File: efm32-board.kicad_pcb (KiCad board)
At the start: 2 copper layers, 18.8 x 51.8 mm, 30 parts, among them J1 Conn_01x20, J2 Conn_01x20, J3 USB_OTG, J4 Conn_02x03_Odd_Even, J5 Conn_01x20, J6 Conn_01x20, SW1 reset, SW2 reset, U1 EFM32HG-48LQFP, U2 SPX3819M5-L-3-3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

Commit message: Add +5v input diode array for split vbus and vin
Signed-off-by: Martin Ribelotta <martinribelotta@gmail.com>
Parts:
- added D2: PMEG2005CT, TO_SOT_Packages_SMD:SOT-23, F.Cu at (131.4, 73.9)
- moved J3 4.27 mm to (125.1, 71.7)
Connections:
- J2 pad 1: +5V -> /vin
- J3 pad 1: +5V -> /vusb
- J5 pad 1: +5V -> /vin
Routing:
- net +5V: track 23.0 -> 14.0 mm
- net /vusb: track 0.00 -> 6.62 mm
- net /vin: track 0.00 -> 4.95 mm
- net /B_USB-: track 4.10 -> 5.93 mm
- net /PF0/SWCLK: track 26.1 -> 24.8 mm
- net +3V3: track 110.5 -> 109.2 mm

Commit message: Corrections and fixeds
Signed-off-by: Martin Ribelotta <martinribelotta@gmail.com>
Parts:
- added C12: 4.7u, Capacitors_SMD:C_0603, F.Cu at (129.2, 86.9)
- moved C7 2.56 mm to (127.8, 86.9)
- moved C6 0.27 mm to (131.5, 91.0)
- moved C8 0.27 mm to (132.8, 91.0)
- moved C9 0.11 mm to (132.1, 89.0)
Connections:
- C7 pad 1: +3V3 -> Net-(C7-Pad1)
- J4 pad 2: +5V -> Net-(J4-Pad2)
- U1 pad 33: +3V3 -> /vusb
- U1 pad 34: +3V3 -> Net-(C7-Pad1)
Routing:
- net /vusb: track 6.62 -> 25.3 mm, vias 0 -> 2
- net +3V3: track 109.2 -> 123.8 mm, vias 1 -> 0
- net +5V: track 14.0 -> 7.17 mm
- net Net-(C7-Pad1): track 0.00 -> 5.86 mm
- net /USB-: track 9.57 -> 10.8 mm
- net /PF0/SWCLK: track 24.8 -> 25.5 mm
- net /USB+: track 9.34 -> 9.85 mm

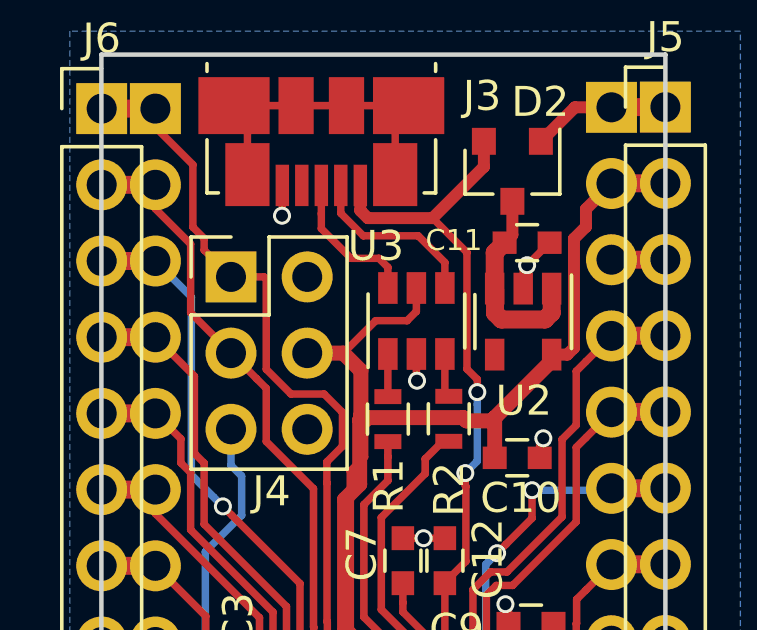
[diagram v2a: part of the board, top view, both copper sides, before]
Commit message: Add jump to pins 2-4 on J4 (SWD)
Signed-off-by: Martin Ribelotta <martinribelotta@gmail.com>
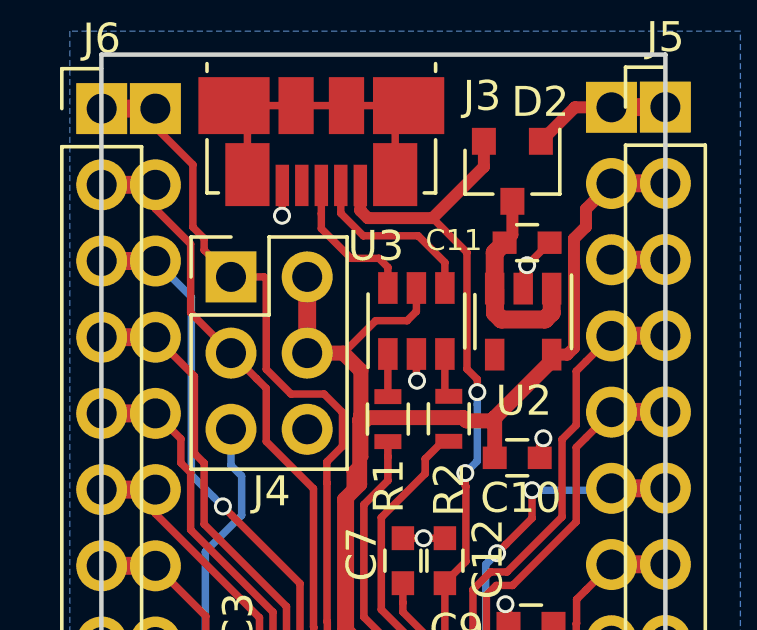
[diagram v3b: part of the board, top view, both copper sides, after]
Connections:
- J4 pad 2: Net-(J4-Pad2) -> +3V3
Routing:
- net +3V3: track 123.8 -> 126.3 mm
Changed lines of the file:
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@@
     (thickness 1.6)
     (drawings 4)
-    (tracks 641)
+    (tracks 642)
     (zones 0)
     (modules 32)
-    (nets 52)
+    (nets 51)
   )
   (page A4)
@@
   (net 49 /vin)
   (net 50 "Net-(C7-Pad1)")
-  (net 51 "Net-(J4-Pad2)")
   (net_class Default "This is the default net class."
     (clearance 0.2)
@@
     (add_net "Net-(D3-Pad2)")
     (add_net "Net-(J3-Pad6)")
-    (add_net "Net-(J4-Pad2)")
     (add_net "Net-(R1-Pad1)")
     (add_net "Net-(R2-Pad1)")
@@
       (net 13 /PF1/SWDIO))
     (pad 2 thru_hole oval (at 2.54 0) (size 1.7 1.7) (drill 1) (layers *.Cu *.Mask)
-      (net 51 "Net-(J4-Pad2)"))
+      (net 3 +3V3))
     (pad 1 thru_hole rect (at 0 0) (size 1.7 1.7) (drill 1) (layers *.Cu *.Mask)
       (net 12 /PF0/SWCLK))
@@
   (segment (start 123.768 75.385) (end 123.758 75.395) (width 0.25) (layer F.Cu) (net 2))
   (via (at 123.758 75.395) (size 0.6) (drill 0.4) (layers F.Cu B.Cu) (net 2))
+  (segment (start 124.598 77.435) (end 124.598 79.975) (width 0.6) (layer F.Cu) (net 3))
   (segment (start 130.848 82.135) (end 130.848 82.13) (width 0.5) (layer F.Cu) (net 3))
   (segment (start 129.798011 82.125001) (end 126.477999 82.125001) (width 0.5) (layer F.Cu) (net 3))

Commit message: Change usb resistors from 22R to 15R
Signed-off-by: Martin Ribelotta <martinribelotta@gmail.com>
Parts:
- R1, R2: value 22R -> 15R
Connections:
- J3 pad 4: (no net) -> Net-(J3-Pad4)
- U2 pad 4: (no net) -> Net-(U2-Pad4)
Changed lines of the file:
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@@
     (zones 0)
     (modules 32)
-    (nets 51)
+    (nets 53)
   )
   (page A4)
@@
   (net 49 /vin)
   (net 50 "Net-(C7-Pad1)")
+  (net 51 "Net-(J3-Pad4)")
+  (net 52 "Net-(U2-Pad4)")
   (net_class Default "This is the default net class."
     (clearance 0.2)
@@
     (add_net "Net-(D1-Pad2)")
     (add_net "Net-(D3-Pad2)")
+    (add_net "Net-(J3-Pad4)")
     (add_net "Net-(J3-Pad6)")
     (add_net "Net-(R1-Pad1)")
     (add_net "Net-(R2-Pad1)")
+    (add_net "Net-(U2-Pad4)")
   )
   (module Capacitors_SMD:C_0603 (layer F.Cu)
@@
     (pad 5 smd rect (at 1.1 -0.95 270) (size 1.06 0.65) (layers F.Cu F.Paste F.Mask)
       (net 3 +3V3))
-    (pad 4 smd rect (at 1.1 0.95 270) (size 1.06 0.65) (layers F.Cu F.Paste F.Mask))
+    (pad 4 smd rect (at 1.1 0.95 270) (size 1.06 0.65) (layers F.Cu F.Paste F.Mask)
+      (net 52 "Net-(U2-Pad4)"))
     (pad 3 smd rect (at -1.1 0.95 270) (size 1.06 0.65) (layers F.Cu F.Paste F.Mask)
       (net 1 +5V))
@@
       (effects (font (size 1 1) (thickness 0.15)))
     )
-    (fp_text value 22R (at 0 1.5 270) (layer F.Fab)
+    (fp_text value 15R (at 0 1.5 270) (layer F.Fab)
       (effects (font (size 1 1) (thickness 0.15)))
     )
@@
       (effects (font (size 1 1) (thickness 0.15)))
     )
-    (fp_text value 22R (at 0 1.5 270) (layer F.Fab)
+    (fp_text value 15R (at 0 1.5 270) (layer F.Fab)
       (effects (font (size 1 1) (thickness 0.15)))
     )
@@
     (pad 5 smd rect (at 1.3 -2.66 180) (size 0.45 1.38) (layers F.Cu F.Paste F.Mask)
       (net 2 GND))
-    (pad 4 smd rect (at 0.65 -2.66 180) (size 0.45 1.38) (layers F.Cu F.Paste F.Mask))
+    (pad 4 smd rect (at 0.65 -2.66 180) (size 0.45 1.38) (layers F.Cu F.Paste F.Mask)
+      (net 51 "Net-(J3-Pad4)"))
     (pad 3 smd rect (at 0 -2.66 180) (size 0.45 1.38) (layers F.Cu F.Paste F.Mask)
       (net 44 /B_USB+))

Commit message: Various fixes for release
Signed-off-by: Martin Ribelotta <martinribelotta@gmail.com>
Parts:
- J4: value Conn_02x03_Odd_Even -> SWD; footprint Pin_Headers:Pin_Header_Straight_2x03_Pitch2.54mm -> Pin_Headers:Pin_Header_Straight_2x02_Pitch2.54mm_SMD
- moved J4 4.23 mm to (123.4, 81.5), turned to 270 degrees
- moved C2 0.31 mm to (121.6, 100.6)
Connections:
- J2 pad 2: +3V3 -> GND
- J2 pad 3: GND -> +3V3
- J3 pad 4: Net-(J3-Pad4) -> (no net)
- J4 pad 2: +3V3 -> GND
- J4 pad 4: +3V3 -> /nRESET
- J5 pad 2: +3V3 -> GND
- J5 pad 3: GND -> +3V3
- U2 pad 4: Net-(U2-Pad4) -> (no net)
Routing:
- net +3V3: track 126.3 -> 119.0 mm
- net /nRESET: track 58.8 -> 55.6 mm, vias 3 -> 4
- net GND: track 36.6 -> 38.6 mm, vias 16 -> 17
- net /PF0/SWCLK: track 25.5 -> 24.5 mm
- net /PF1/SWDIO: track 21.4 -> 22.1 mm
- net /PF2: track 19.1 -> 19.4 mm, vias 1 -> 0
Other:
- board text added: "PA7"
- board text added: "PB8"
- board text added: "PWR"
- board text added: "RST"

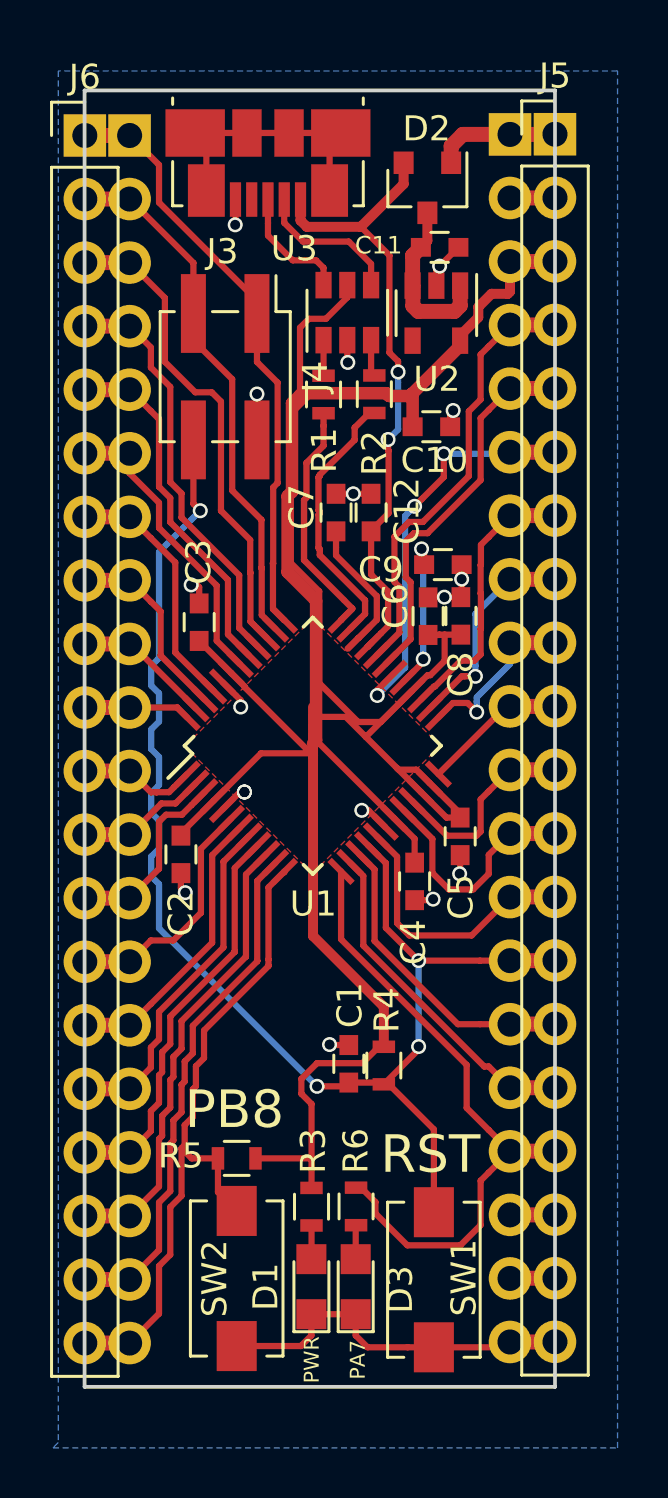
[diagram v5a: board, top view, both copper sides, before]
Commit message: Add +3v3 on pin 18 (previous GND) for prototyping convenience
Signed-off-by: Martin Ribelotta <martinribelotta@gmail.com>
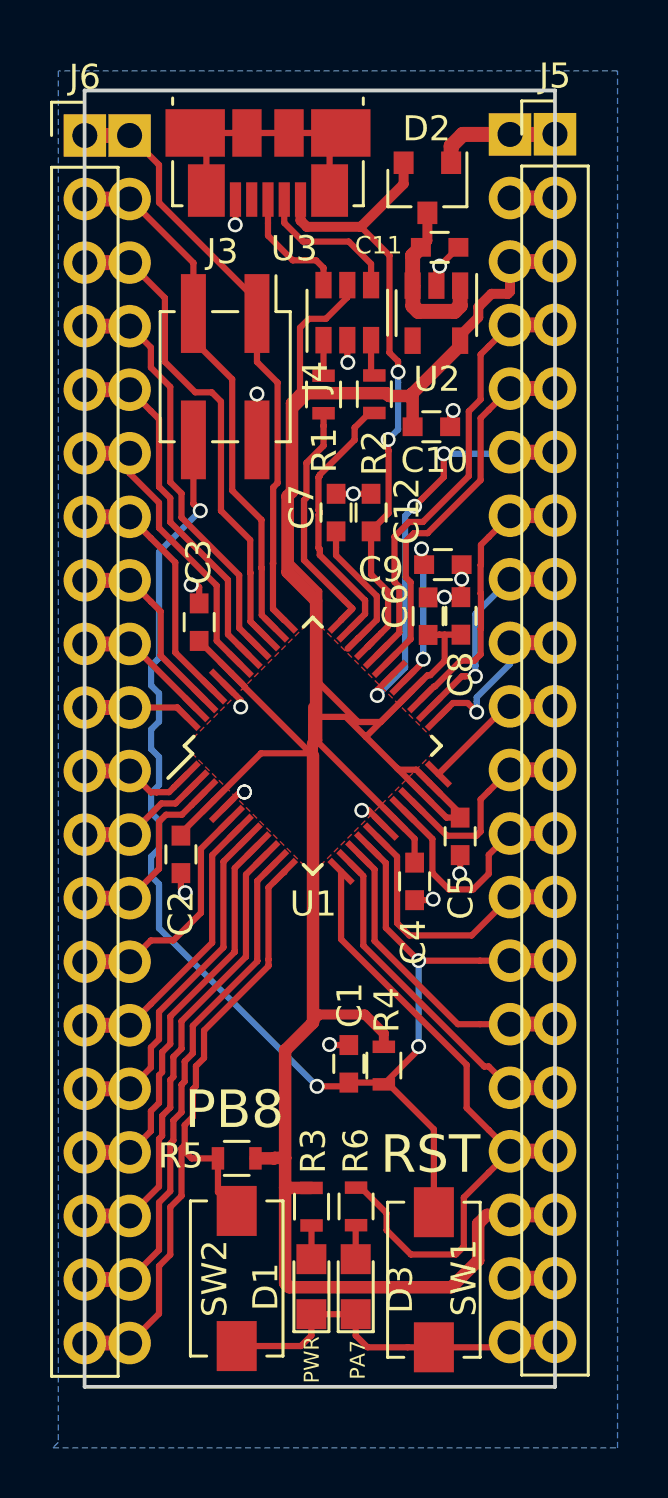
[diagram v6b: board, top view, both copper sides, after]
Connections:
- J2 pad 18: GND -> +3V3
- J5 pad 18: GND -> +3V3
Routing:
- net +3V3: track 119.0 -> 136.2 mm
- net GND: track 38.6 -> 36.8 mm
- net /PA8: track 25.8 -> 26.3 mm
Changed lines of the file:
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@@
     (thickness 1.6)
     (drawings 8)
-    (tracks 663)
+    (tracks 671)
     (zones 0)
     (modules 32)
@@
       (net 32 /PA8))
     (pad 18 thru_hole oval (at 0 43.18) (size 1.7 1.7) (drill 1) (layers *.Cu *.Mask)
-      (net 2 GND))
+      (net 3 +3V3))
     (pad 19 thru_hole oval (at 0 45.72) (size 1.7 1.7) (drill 1) (layers *.Cu *.Mask)
       (net 2 GND))
@@
       (net 32 /PA8))
     (pad 18 thru_hole oval (at 0 -43.18 180) (size 1.7 1.7) (drill 1) (layers *.Cu *.Mask)
-      (net 2 GND))
+      (net 3 +3V3))
     (pad 19 thru_hole oval (at 0 -45.72 180) (size 1.7 1.7) (drill 1) (layers *.Cu *.Mask)
       (net 2 GND))
@@
   (segment (start 123.768 75.385) (end 123.758 75.395) (width 0.25) (layer F.Cu) (net 2))
   (via (at 123.758 75.395) (size 0.6) (drill 0.4) (layers F.Cu B.Cu) (net 2))
+  (segment (start 134.740619 114.9625) (end 136.5305 114.9625) (width 0.6) (layer F.Cu) (net 3))
+  (segment (start 136.5305 114.9625) (end 136.538 114.955) (width 0.6) (layer F.Cu) (net 3))
+  (segment (start 132.398 117.855) (end 133.468 116.785) (width 0.5) (layer F.Cu) (net 3))
+  (segment (start 133.468 116.785) (end 133.468 115.315) (width 0.5) (layer F.Cu) (net 3))
+  (segment (start 125.753 113.875) (end 125.753 117.692501) (width 0.5) (layer F.Cu) (net 3))
+  (segment (start 125.753 117.692501) (end 125.915499 117.855) (width 0.5) (layer F.Cu) (net 3))
+  (segment (start 133.468 115.315) (end 133.8205 114.9625) (width 0.5) (layer F.Cu) (net 3))
+  (segment (start 125.915499 117.855) (end 132.398 117.855) (width 0.5) (layer F.Cu) (net 3))
+  (segment (start 133.8205 114.9625) (end 134.740619 114.9625) (width 0.5) (layer F.Cu) (net 3))
+  (segment (start 126.868 107.215) (end 126.868 107.275) (width 0.5) (layer F.Cu) (net 3))
+  (segment (start 125.753 108.39) (end 125.753 112.685) (width 0.5) (layer F.Cu) (net 3))
+  (segment (start 126.868 107.275) (end 125.753 108.39) (width 0.5) (layer F.Cu) (net 3))
+  (segment (start 129.698 107.715) (end 129.698 108.245) (width 0.4) (layer F.Cu) (net 3))
+  (segment (start 128.938 106.955) (end 129.698 107.715) (width 0.4) (layer F.Cu) (net 3))
+  (segment (start 127.128 106.955) (end 128.938 106.955) (width 0.4) (layer F.Cu) (net 3))
+  (segment (start 126.868 107.215) (end 127.128 106.955) (width 0.4) (layer F.Cu) (net 3))
+  (segment (start 126.868 96.605) (end 126.868 107.215) (width 0.5) (layer F.Cu) (net 3))
+  (segment (start 125.753 112.685) (end 125.753 113.875) (width 0.5) (layer F.Cu) (net 3))
+  (segment (start 124.568 112.705) (end 125.318 112.705) (width 0.5) (layer F.Cu) (net 3))
+  (segment (start 125.318 112.705) (end 125.338 112.685) (width 0.5) (layer F.Cu) (net 3))
+  (segment (start 125.338 112.685) (end 125.753 112.685) (width 0.5) (layer F.Cu) (net 3))
+  (segment (start 125.763 113.885) (end 125.753 113.875) (width 0.5) (layer F.Cu) (net 3))
+  (segment (start 126.808 113.885) (end 125.763 113.885) (width 0.5) (layer F.Cu) (net 3))
   (segment (start 122.898202 98.407031) (end 121.588 99.717233) (width 0.25) (layer F.Cu) (net 3))
   (segment (start 121.588 99.717233) (end 121.588 99.805) (width 0.25) (layer F.Cu) (net 3))
@@
   (segment (start 120.778 90.845) (end 120.387999 90.454999) (width 0.25) (layer F.Cu) (net 19))
   (segment (start 120.387999 90.454999) (end 119.538 89.605) (width 0.25) (layer F.Cu) (net 19))
+  (segment (start 133.89062 113.272499) (end 134.740619 112.4225) (width 0.25) (layer F.Cu) (net 32))
+  (segment (start 132.578 116.545) (end 132.892989 116.230011) (width 0.25) (layer F.Cu) (net 32))
+  (segment (start 130.778 116.545) (end 132.578 116.545) (width 0.25) (layer F.Cu) (net 32))
+  (segment (start 129.808 115.575) (end 130.778 116.545) (width 0.25) (layer F.Cu) (net 32))
+  (segment (start 129.808 114.895) (end 129.808 115.575) (width 0.25) (layer F.Cu) (net 32))
+  (segment (start 132.892989 114.27013) (end 133.89062 113.272499) (width 0.25) (layer F.Cu) (net 32))
+  (segment (start 128.788 113.875) (end 129.808 114.895) (width 0.25) (layer F.Cu) (net 32))
+  (segment (start 128.588 113.875) (end 128.788 113.875) (width 0.25) (layer F.Cu) (net 32))
+  (segment (start 132.892989 116.230011) (end 132.892989 114.27013) (width 0.25) (layer F.Cu) (net 32))
   (segment (start 127.5305 74.025) (end 127.5305 72.1725) (width 0.25) (layer F.Cu) (net 38) (status 30))
   (segment (start 127.5305 72.1725) (end 127.978 71.725) (width 0.25) (layer F.Cu) (net 38) (status 30))
@@
   (segment (start 136.538 117.495) (end 134.748119 117.495) (width 0.6) (layer F.Cu) (net 2) (status 30))
   (segment (start 134.748119 117.495) (end 134.740619 117.5025) (width 0.6) (layer F.Cu) (net 2) (status 30))
-  (segment (start 134.740619 114.9625) (end 136.5305 114.9625) (width 0.6) (layer F.Cu) (net 2) (status 30))
-  (segment (start 136.5305 114.9625) (end 136.538 114.955) (width 0.6) (layer F.Cu) (net 2) (status 30))
   (segment (start 132.348 83.465) (end 132.348 82.935) (width 0.25) (layer F.Cu) (net 2) (status 10))
   (segment (start 132.348 82.935) (end 132.468 82.815) (width 0.25) (layer F.Cu) (net 2))
   (via (at 132.468 82.815) (size 0.6) (drill 0.4) (layers F.Cu B.Cu) (net 2))
-  (segment (start 126.808 113.885) (end 126.808 112.715) (width 0.25) (layer F.Cu) (net 3) (status 10))
-  (segment (start 126.808 112.715) (end 126.808 110.530002) (width 0.25) (layer F.Cu) (net 3))
-  (segment (start 124.568 112.705) (end 126.798 112.705) (width 0.25) (layer F.Cu) (net 3) (status 10))
-  (segment (start 126.798 112.705) (end 126.808 112.715) (width 0.25) (layer F.Cu) (net 3))
-  (segment (start 126.808 110.530002) (end 126.402999 110.125001) (width 0.25) (layer F.Cu) (net 3))
-  (segment (start 126.402999 110.125001) (end 126.402999 109.524999) (width 0.25) (layer F.Cu) (net 3))
-  (segment (start 126.402999 109.524999) (end 127.027997 108.900001) (width 0.25) (layer F.Cu) (net 3))
-  (segment (start 127.027997 108.900001) (end 128.842999 108.900001) (width 0.25) (layer F.Cu) (net 3))
-  (segment (start 128.842999 108.900001) (end 129.498 108.245) (width 0.25) (layer F.Cu) (net 3) (status 20))
   (segment (start 129.498 108.245) (end 129.698 108.245) (width 0.25) (layer F.Cu) (net 3) (status 30))
-  (segment (start 129.698 106.645) (end 129.698 107.345) (width 0.4) (layer F.Cu) (net 3))
-  (segment (start 129.698 107.345) (end 129.698 108.245) (width 0.4) (layer F.Cu) (net 3) (status 20))
   (segment (start 130.848 83.465) (end 130.848 82.135) (width 0.5) (layer F.Cu) (net 3) (status 10))
   (segment (start 134.748119 74.315) (end 134.740619 74.3225) (width 0.6) (layer F.Cu) (net 2) (status 30))
@@
   (segment (start 132.748 101.31) (end 132.728 101.33) (width 0.25) (layer F.Cu) (net 2))
   (via (at 132.728 101.33) (size 0.6) (drill 0.4) (layers F.Cu B.Cu) (net 2))
-  (segment (start 126.868 96.605) (end 126.868 103.815) (width 0.4) (layer F.Cu) (net 3))
-  (segment (start 126.868 103.815) (end 129.698 106.645) (width 0.4) (layer F.Cu) (net 3))
   (segment (start 123.605309 93.315862) (end 123.605309 93.312309) (width 0.25) (layer F.Cu) (net 3) (status 30))
   (segment (start 123.605309 93.312309) (end 122.318 92.025) (width 0.25) (layer F.Cu) (net 3) (status 30))
@@
   (segment (start 117.748 112.465) (end 119.538 112.465) (width 0.6) (layer F.Cu) (net 28) (status 30))
   (segment (start 125.726629 101.276371) (end 125.726629 101.235458) (width 0.25) (layer F.Cu) (net 31) (status 30))
-  (segment (start 128.588 113.875) (end 128.788 113.875) (width 0.25) (layer F.Cu) (net 32) (status 30))
-  (segment (start 128.788 113.875) (end 129.363001 114.450001) (width 0.25) (layer F.Cu) (net 32) (status 10))
-  (segment (start 130.637999 116.180001) (end 132.758001 116.180001) (width 0.25) (layer F.Cu) (net 32))
-  (segment (start 129.363001 114.450001) (end 129.363001 114.905003) (width 0.25) (layer F.Cu) (net 32))
-  (segment (start 129.363001 114.905003) (end 130.637999 116.180001) (width 0.25) (layer F.Cu) (net 32))
-  (segment (start 132.758001 116.180001) (end 133.565618 115.372384) (width 0.25) (layer F.Cu) (net 32))
-  (segment (start 133.565618 115.372384) (end 133.565618 113.597501) (width 0.25) (layer F.Cu) (net 32))
-  (segment (start 133.565618 113.597501) (end 133.89062 113.272499) (width 0.25) (layer F.Cu) (net 32))
-  (segment (start 133.89062 113.272499) (end 134.740619 112.4225) (width 0.25) (layer F.Cu) (net 32) (status 20))
   (segment (start 128.588 113.875) (end 128.612998 113.875) (width 0.25) (layer F.Cu) (net 32) (status 30))
   (segment (start 136.538 112.415) (end 134.748119 112.415) (width 0.6) (layer F.Cu) (net 32) (status 30))
